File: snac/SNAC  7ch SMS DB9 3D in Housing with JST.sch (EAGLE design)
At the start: 42 parts, among them IC1 4030D, Q1 BSS138, Q2 BSS138, Q3 BSS138, Q4 BSS138, Q5 BSS138, Q6 BSS138, Q7 BSS138, Q8 BSS138, Q9 BC849SMD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

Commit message: Updated SMS DB9 with JST version, and PCB image
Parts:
- removed JP3: (no value), SparkFun:JUMPER-2PTH
- added JP1: JUMPER-SMT_2_NC_TRACE_SILK, SparkFun-Jumpers:JUMPER-SMT_2_NC_TRACE_SILK
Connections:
- net J1: now also JP1.1, X4-9.S, X5-9.S; no longer JP3.1
- net LV7: now also JP1.2; no longer JP3.2, X4-9.S, X5-9.S
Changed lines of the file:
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@@
 <layer number="112" name="tSilk" color="7" fill="1" visible="yes" active="yes"/>
 <layer number="113" name="IDFDebug" color="4" fill="1" visible="yes" active="yes"/>
+<layer number="114" name="Badge_Outline" color="7" fill="1" visible="no" active="no"/>
+<layer number="115" name="ReferenceISLANDS" color="7" fill="1" visible="no" active="no"/>
 <layer number="116" name="Patch_BOT" color="9" fill="4" visible="no" active="yes"/>
 <layer number="118" name="Rect_Pads" color="7" fill="1" visible="no" active="no"/>
@@
 <part name="X1" library="Rembrandt Electronics - JST XH Connectors v1-0" deviceset="JST-XH-02-PIN" device="-ROUND-PAD" value="JST-XH-02-PIN-ROUND-PAD"/>
 <part name="U1" library="PMIC-LDO-XC6206P332MR-G_SOT23_" deviceset="PMIC-LDO-XC6206P332MR-G(SOT23)" device=""/>
-<part name="JP3" library="SparkFun" deviceset="JUMPER-2" device="PTH"/>
 <part name="IC1" library="40xx" deviceset="4030" device="D"/>
 <part name="R17" library="SparkFun" deviceset="RESISTOR" device="0603-RES" value="22K"/>
@@
 <part name="X4" library="Rembrandt Electronics - JST XH Connectors v1-0" deviceset="JST-XH-09-PIN" device="-LONG-PAD"/>
 <part name="X5" library="Rembrandt Electronics - JST XH Connectors v1-0" deviceset="JST-XH-09-PIN" device="-LONG-PAD"/>
+<part name="JP1" library="SparkFun-Jumpers" deviceset="JUMPER-SMT_2_NC_TRACE" device="_SILK" package3d_urn="urn:adsk.eagle:package:39281/1"/>
 </parts>
 <sheets>
@@
 <instance part="X1" gate="-1" x="55.88" y="22.86"/>
 <instance part="U1" gate="G$1" x="124.46" y="91.44"/>
-<instance part="JP3" gate="A" x="162.56" y="91.44"/>
 <instance part="IC1" gate="A" x="360.68" y="86.36"/>
 <instance part="IC1" gate="B" x="388.62" y="71.12"/>
@@
 <instance part="X5" gate="-8" x="55.245" y="39.37"/>
 <instance part="X5" gate="-9" x="55.245" y="36.83"/>
+<instance part="JP1" gate="G$1" x="104.14" y="30.48"/>
 </instances>
 <busses>
@@
 </segment>
 <segment>
-<pinref part="JP3" gate="A" pin="2"/>
-<wire x1="165.1" y1="88.9" x2="165.1" y2="83.82" width="0.1524" layer="91"/>
-<label x="165.1" y="83.82" size="1.27" layer="95" xref="yes"/>
-</segment>
-<segment>
 <pinref part="R20" gate="G$1" pin="1"/>
 <wire x1="340.36" y1="38.1" x2="330.2" y2="38.1" width="0.1524" layer="91"/>
@@
 </segment>
 <segment>
-<wire x1="52.705" y1="69.85" x2="47.625" y2="69.85" width="0.1524" layer="91"/>
-<label x="47.625" y="69.85" size="1.27" layer="95" rot="MR0" xref="yes"/>
-<pinref part="X4" gate="-9" pin="S"/>
-</segment>
-<segment>
-<wire x1="52.705" y1="36.83" x2="47.625" y2="36.83" width="0.1524" layer="91"/>
-<label x="47.625" y="36.83" size="1.27" layer="95" rot="MR0" xref="yes"/>
-<pinref part="X5" gate="-9" pin="S"/>
+<pinref part="JP1" gate="G$1" pin="2"/>
+<wire x1="109.22" y1="30.48" x2="116.84" y2="30.48" width="0.1524" layer="91"/>
+<label x="111.76" y="30.48" size="1.778" layer="95"/>
 </segment>
 </net>
@@
 <label x="47.625" y="49.53" size="1.27" layer="95" rot="MR0" xref="yes"/>
 <pinref part="X5" gate="-4" pin="S"/>
-</segment>
-</net>
-<net name="J1" class="0">
-<segment>
-<pinref part="JP3" gate="A" pin="1"/>
-<wire x1="162.56" y1="88.9" x2="162.56" y2="83.82" width="0.1524" layer="91"/>
-<label x="162.56" y="83.82" size="1.27" layer="95" rot="MR0" xref="yes"/>
 </segment>
 </net>
@@
 </segment>
 </net>
+<net name="J1" class="0">
+<segment>
+<wire x1="52.705" y1="36.83" x2="47.625" y2="36.83" width="0.1524" layer="91"/>
+<label x="47.625" y="36.83" size="1.27" layer="95" rot="MR0" xref="yes"/>
+<pinref part="X5" gate="-9" pin="S"/>
+</segment>
+<segment>
+<pinref part="JP1" gate="G$1" pin="1"/>
+<wire x1="99.06" y1="30.48" x2="91.44" y2="30.48" width="0.1524" layer="91"/>
+<label x="93.98" y="30.48" size="1.778" layer="95"/>
+</segment>
+<segment>
+<wire x1="52.705" y1="69.85" x2="47.625" y2="69.85" width="0.1524" layer="91"/>
+<label x="47.625" y="69.85" size="1.27" layer="95" rot="MR0" xref="yes"/>
+<pinref part="X4" gate="-9" pin="S"/>
+</segment>
+</net>

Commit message: changed from LV7 to LV5 pin on the DB9 3D with JST design
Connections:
- net LV5: now also R20.1
- net LV7: no longer R20.1
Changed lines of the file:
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@@
 <setting verticaltext="up"/>
 </settings>
-<grid distance="0.1" unitdist="inch" unit="inch" style="lines" multiple="1" display="no" altdistance="0.01" altunitdist="inch" altunit="inch"/>
+<grid distance="100" unitdist="mil" unit="mil" style="lines" multiple="1" display="no" altdistance="0.01" altunitdist="inch" altunit="inch"/>
 <layers>
 <layer number="1" name="Top" color="4" fill="1" visible="no" active="no"/>
@@
 <pinref part="X5" gate="-6" pin="S"/>
 </segment>
+<segment>
+<pinref part="R20" gate="G$1" pin="1"/>
+<wire x1="340.36" y1="38.1" x2="330.2" y2="38.1" width="0.1524" layer="91"/>
+<label x="335.28" y="38.1" size="1.778" layer="95" rot="MR0"/>
+</segment>
 </net>
 <net name="HV5" class="0">
@@
 </segment>
 <segment>
-<pinref part="R20" gate="G$1" pin="1"/>
-<wire x1="340.36" y1="38.1" x2="330.2" y2="38.1" width="0.1524" layer="91"/>
-<label x="335.28" y="38.1" size="1.778" layer="95" rot="MR0"/>
-</segment>
-<segment>

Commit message: Added charge pump to the SMS 3D and SMS DB9 3D PCBs
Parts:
- removed D2: BAT54, diode:BAT54
- removed R18: 47K, pot:TRIM_EU-B25P
- added C10, C11, C7, C8, C9: 2.2uF, rc-master-smd:C_0805
- added C12: 10nF, rc-master-smd:C_0805
- added C13: 22uF, rc-master-smd:C_0805
- added D3, D4: BAS40-04, diode:BAS40-04
- added IC3: 4030D, 40xx:4030D
- added R24: 75K, SparkFun:RESISTOR0603-RES
- R17: value 22K -> 75K
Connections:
- removed net N$10: IC1D.I1, R17.2
- new net 10V: C4.1, C7.1, D4.C2, IC1A.I0, IC1C.I1, IC1D.I0, IC1P.VDD, R19.1
- new net N$27: C9.1, D3.C2, D4.A1
- new net N$28: C8.1, D3.A1
- new net N$29: C11.2, D4.C1A2
- new net N$30: C10.2, D3.C1A2
- new net N$31: C12.1, IC3A.I1, IC3D.O, R24.2
- new net N$32: IC3D.I1, R24.1
- new net N$33: C10.1, C11.1, IC3B.O
- new net N$34: C12.2, IC3A.O, IC3B.I0, IC3B.I1
- net GND: now also C13.2, C8.2, IC3C.I0, IC3C.I1, IC3P.VSS; no longer D2.A
- net HV: now also C13.1, C7.2, C9.2, IC3A.I0, IC3D.I0, IC3P.VDD; no longer C4.1, IC1A.I0, IC1C.I1, IC1D.I0, IC1P.VDD, R19.1
- net LV5: no longer R20.1
- net LV6: now also R20.1
- net N$14: no longer D2.C
- net N$5: now also C3.1, R17.2; no longer R18.A, R18.S
- net N$9: now also IC1D.I1; no longer C3.1, R18.E
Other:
- note added: ""USB 3.0" SKT..."
- note added: "(IOB P7)"
- note added: "1. VBUS"
- note added: "2. D-"
- note added: "3. D+"
- note added: "4. GND"
- note added: "5. SSRX-"
- note added: "6. SSRX+"
- note added: "7. GND_DRAIN"
- note added: "8. SSTX-"
- note added: "9. SSTX+"
- note added: "Arduino_IO10"
- note added: "Arduino_IO11"
- note added: "Arduino_IO12"
- note added: "Arduino_IO13"
- note added: "Arduino_IO14"
- note added: "Arduino_IO15"
- note added: "Arduino_IO8"
- note added: "Arduino_IO9"
- note added: "Arduino_VREF"
- note added: "CTS"
- note added: "Core name..."
- note added: "DE10 Name..."
- note added: "DSR"
- note added: "DTR"
- note added: "FPGA PIN..."
- note added: "GND"
- note added: "IO6"
- note added: "IOB NAME..."
- note added: "JP2 PIN1"
- note added: "JP2 PIN10"
- note added: "JP2 PIN2"
- note added: "JP2 PIN3"
- note added: "JP2 PIN4"
- note added: "JP2 PIN5"
- note added: "JP2 PIN6"
- note added: "JP2 PIN7"
- note added: "JP2 PIN8"
- note added: "JP2 PIN9"
- note added: "PIN_AE15"
- note added: "PIN_AF15"
- note added: "PIN_AF17"
- note added: "PIN_AG11"
- note added: "PIN_AG16"
- note added: "PIN_AH11"
- note added: "PIN_AH12"
- note added: "PIN_AH9"
- note added: "RTS"
- note added: "RX"
- note added: "SOG"
- note added: "TX"
- note added: "USERIO NAME..."
- note added: "USERIO_LV1"
- note added: "USERIO_LV2"
- note added: "USERIO_LV3"
- note added: "USERIO_LV4"
- note added: "USERIO_LV5"
- note added: "USERIO_LV6"
- note added: "USERIO_LV7"
- note added: "USER_IO[0]"
- note added: "USER_IO[1]"
- note added: "USER_IO[2]"
- note added: "USER_IO[3]"
- note added: "USER_IO[4]"
- note added: "USER_IO[5]"
- note added: "USER_IO[6]"

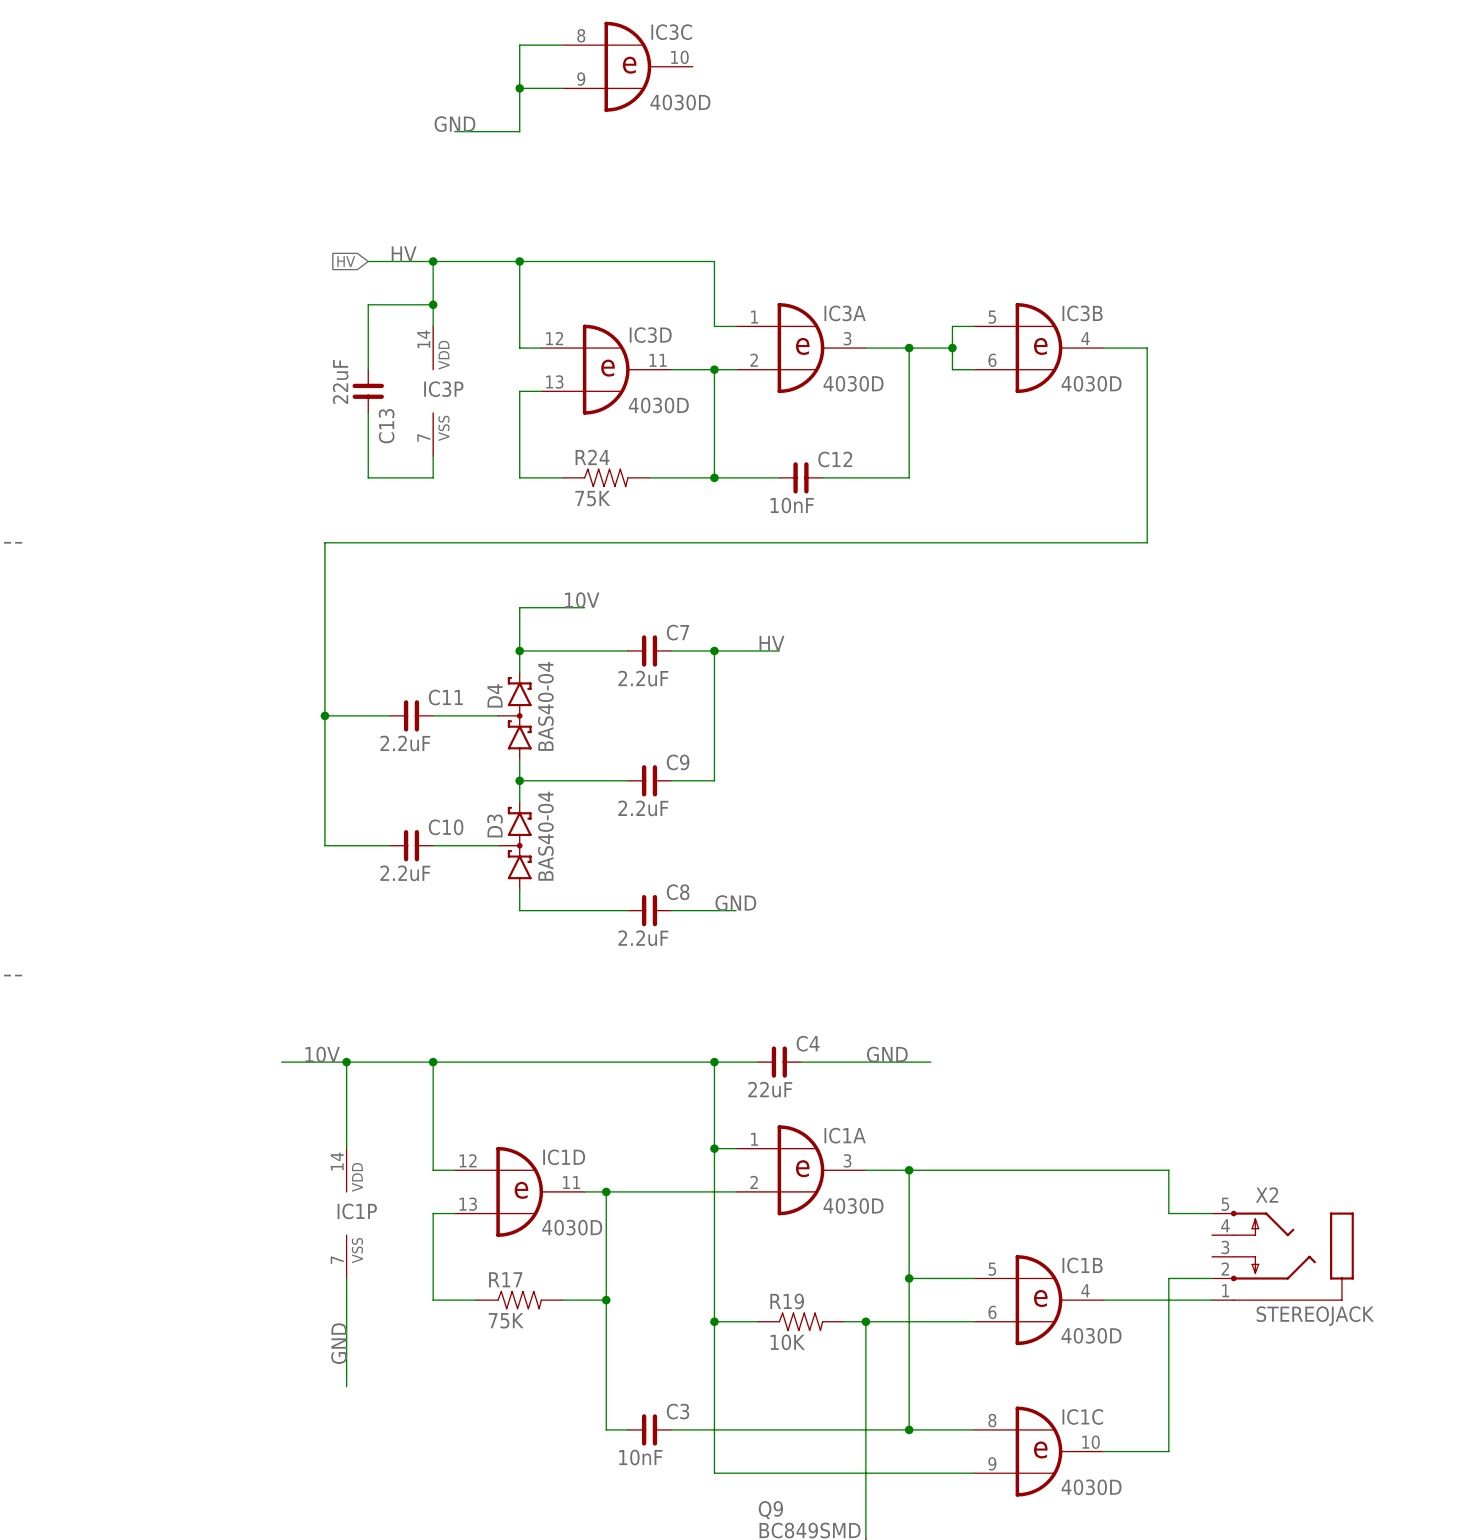
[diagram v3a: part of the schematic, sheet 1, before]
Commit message: Changed to a MAX660 charge pump on the JST DB9 3D Glasses board
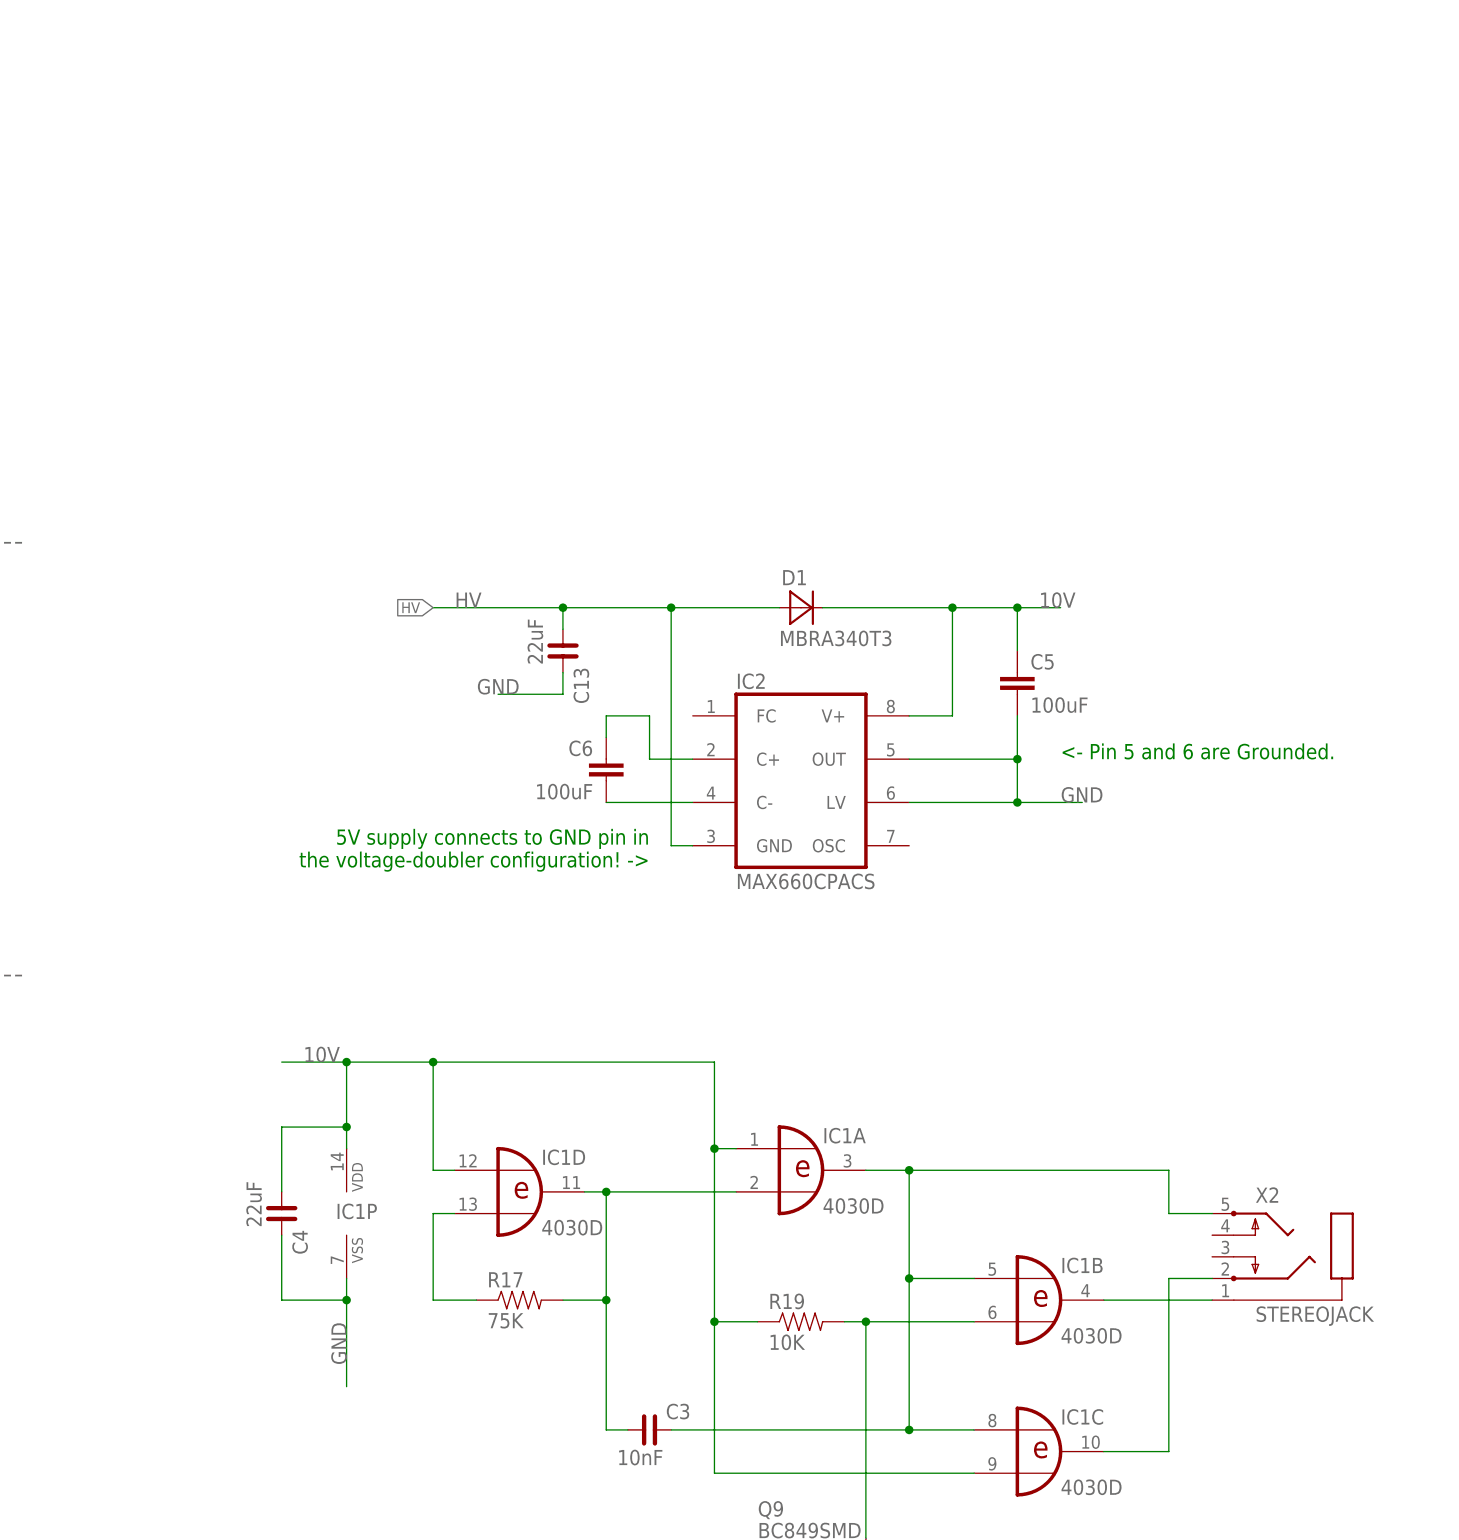
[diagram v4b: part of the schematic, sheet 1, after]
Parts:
- removed C10, C11, C7, C8, C9: 2.2uF, rc-master-smd:C_0805
- removed C12: 10nF, rc-master-smd:C_0805
- removed D3, D4: BAS40-04, diode:BAS40-04
- removed IC3: 4030D, 40xx:4030D
- removed R24: 75K, SparkFun:RESISTOR0603-RES
- added C5, C6: 100uF, rcl:C-EUC1812
- added D1: MBRA340T3, diode:MBRA340T3
- added IC2: MAX660CPACS, maxim:MAX660CPACS
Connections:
- removed net N$27: C9.1, D3.C2, D4.A1
- removed net N$28: C8.1, D3.A1
- removed net N$29: C11.2, D4.C1A2
- removed net N$30: C10.2, D3.C1A2
- removed net N$31: C12.1, IC3A.I1, IC3D.O, R24.2
- removed net N$32: IC3D.I1, R24.1
- removed net N$33: C10.1, C11.1, IC3B.O
- removed net N$34: C12.2, IC3A.O, IC3B.I0, IC3B.I1
- new net N$10: C6.1, IC2.C+
- new net N$23: C6.2, IC2.C-
- net 10V: now also C5.1, D1.C, IC2.V+; no longer C7.1, D4.C2
- net GND: now also C5.2, IC2.LV, IC2.OUT; no longer C8.2, IC3C.I0, IC3C.I1, IC3P.VSS
- net HV: now also D1.A, IC2.GND; no longer C7.2, C9.2, IC3A.I0, IC3D.I0, IC3P.VDD
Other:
- note added: "5V supply connects to GND pin in the voltage-doubler configuration! ->"
- note added: "<- Pin 5 and 6 are Grounded."
- moved on the sheet: C13, C4
